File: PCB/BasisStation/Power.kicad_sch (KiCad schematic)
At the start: 5 parts, among them SW1 SW_SPST

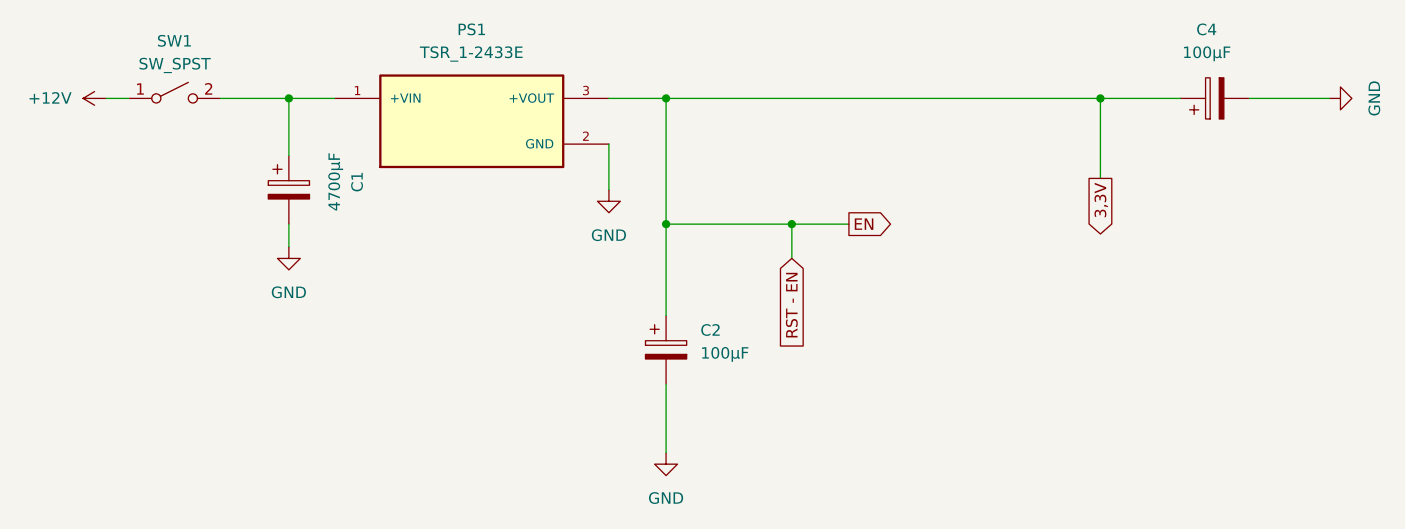
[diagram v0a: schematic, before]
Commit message: Schaltplan angepasst
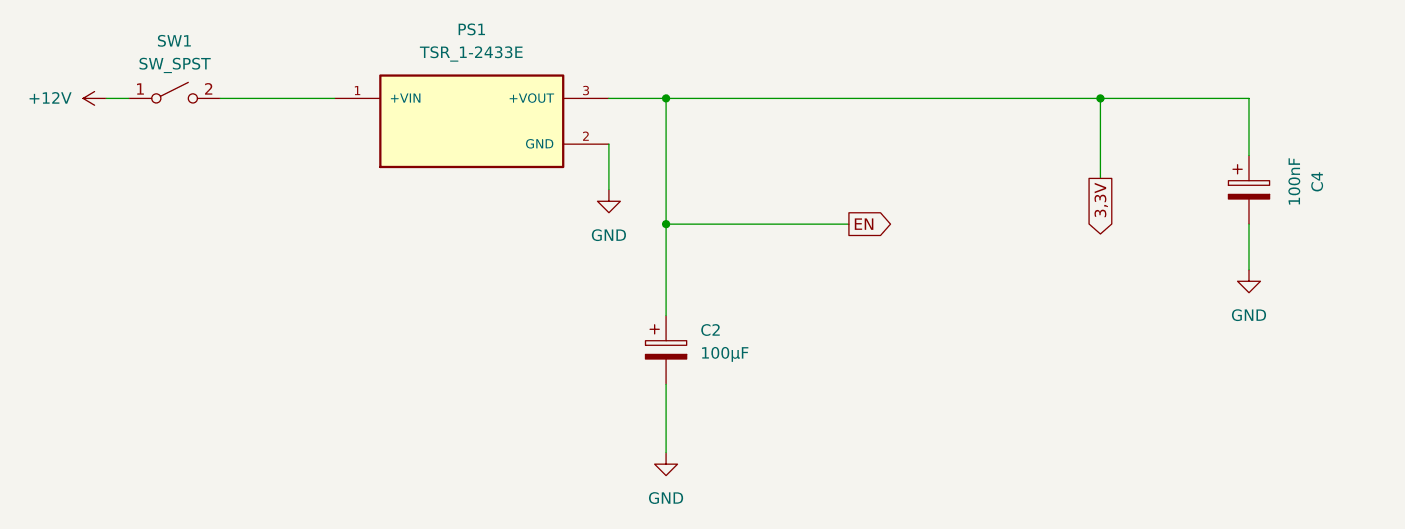
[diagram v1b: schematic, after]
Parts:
- removed C1: 4700µF, CUSTOM_Footprint:CAPAE530X565N, symbol Device:C_Polarized
- C4: value 100µF -> 100nF
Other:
- moved on the sheet: C4
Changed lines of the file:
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@@
-	)
-	(junction
-		(at 115.57 114.3)
-		(diameter 0)
-		(color 0 0 0 0)
-	)
-	(junction
-		(at 59.69 100.33)
-		(diameter 0)
-		(color 0 0 0 0)
 	)
 	(junction
@@
 	(wire
 		(pts
-			(xy 101.6 114.3) (xy 115.57 114.3)
-		)
-		(stroke
-			(width 0)
-			(type default)
-		)
-	)
-	(wire
-		(pts
-			(xy 59.69 100.33) (xy 59.69 106.68)
+			(xy 101.6 114.3) (xy 121.92 114.3)
 		)
 		(stroke
@@
 	(wire
 		(pts
-			(xy 59.69 100.33) (xy 64.77 100.33)
+			(xy 52.07 100.33) (xy 64.77 100.33)
 		)
 		(stroke
@@
 	(wire
 		(pts
-			(xy 52.07 100.33) (xy 59.69 100.33)
-		)
-		(stroke
-			(width 0)
-			(type default)
-		)
-	)
-	(wire
-		(pts
-			(xy 115.57 114.3) (xy 115.57 118.11)
+			(xy 166.37 106.68) (xy 166.37 100.33)
 		)
 		(stroke
@@
 	(wire
 		(pts
-			(xy 121.92 114.3) (xy 115.57 114.3)
-		)
-		(stroke
-			(width 0)
-			(type default)
-		)
-	)
-	(wire
-		(pts
 			(xy 101.6 114.3) (xy 101.6 124.46)
 		)
@@
 	(wire
 		(pts
-			(xy 166.37 100.33) (xy 175.26 100.33)
-		)
-		(stroke
-			(width 0)
-			(type default)
-		)
-	)
-	(wire
-		(pts
 			(xy 95.25 100.33) (xy 101.6 100.33)
 		)
@@
 	(wire
 		(pts
-			(xy 149.86 100.33) (xy 158.75 100.33)
-		)
-		(stroke
-			(width 0)
-			(type default)
-		)
-	)
-	(wire
-		(pts
-			(xy 59.69 116.84) (xy 59.69 114.3)
+			(xy 149.86 100.33) (xy 166.37 100.33)
+		)
+		(stroke
+			(width 0)
+			(type default)
+		)
+	)
+	(wire
+		(pts
+			(xy 166.37 114.3) (xy 166.37 119.38)
 		)
 		(stroke
@@
 				)
 				(justify left)
-				(hide yes)
-			)
-		)
-	)
-	(global_label "RST - EN"
-		(shape input)
-		(at 115.57 118.11 270)
-		(fields_autoplaced yes)
-		(effects
-			(font
-				(size 1.27 1.27)
-			)
-			(justify right)
-		)
-		(property "Intersheetrefs" "${INTERSHEET_REFS}"
-			(at 115.57 130.5294 90)
-			(effects
-				(font
-					(size 1.27 1.27)
-				)
-				(justify right)
 				(hide yes)
 			)
@@
 	)
 	(symbol
-		(lib_id "power:GND")
-		(at 59.69 116.84 0)
-		(unit 1)
-		(exclude_from_sim no)
-		(in_bom yes)
-		(on_board yes)
-		(dnp no)
-		(fields_autoplaced yes)
-		(property "Reference" "#PWR03"
-			(at 59.69 123.19 0)
-			(effects
-				(font
-					(size 1.27 1.27)
-				)
-				(hide yes)
-			)
-		)
-		(property "Value" "GND"
-			(at 59.69 121.92 0)
-			(effects
-				(font
-					(size 1.27 1.27)
-				)
-			)
-		)
-		(property "Footprint" ""
-			(at 59.69 116.84 0)
-			(effects
-				(font
-					(size 1.27 1.27)
-				)
-				(hide yes)
-			)
-		)
-		(property "Datasheet" ""
-			(at 59.69 116.84 0)
-			(effects
-				(font
-					(size 1.27 1.27)
-				)
-				(hide yes)
-			)
-		)
-		(property "Description" "Power symbol creates a global label with name \"GND\" , ground"
-			(at 59.69 116.84 0)
-			(effects
-				(font
-					(size 1.27 1.27)
-				)
-				(hide yes)
-			)
-		)
-		(pin "1"
-		)
-		(instances
-			(project "BasisStation"
-				(path "/cc03a18a-a128-4e00-a998-441923eeacd1/95bbc6e9-cea3-48d2-a467-ede743e61415"
-					(reference "#PWR03")
-					(unit 1)
-				)
-			)
-		)
-	)
-	(symbol
-		(lib_id "Device:C_Polarized")
-		(at 59.69 110.49 0)
-		(unit 1)
-		(exclude_from_sim no)
-		(in_bom yes)
-		(on_board yes)
-		(dnp no)
-		(fields_autoplaced yes)
-		(property "Reference" "C1"
-			(at 67.31 109.601 90)
-			(effects
-				(font
-					(size 1.27 1.27)
-				)
-			)
-		)
-		(property "Value" "4700µF"
-			(at 64.77 109.601 90)
-			(effects
-				(font
-					(size 1.27 1.27)
-				)
-			)
-		)
-		(property "Footprint" "CUSTOM_Footprint:CAPAE530X565N"
-			(at 60.6552 114.3 0)
-			(effects
-				(font
-					(size 1.27 1.27)
-				)
-				(hide yes)
-			)
-		)
-		(property "Datasheet" "https://www.mouser.de/c/passive-components/capacitors/aluminum-electrolytic-capacitors/aluminum-electrolytic-capacitors-smd/?capacitance=4700%20uF&m=Wurth%20Elektronik"
-			(at 59.69 110.49 0)
-			(effects
-				(font
-					(size 1.27 1.27)
-				)
-				(hide yes)
-			)
-		)
-		(property "Description" "Polarized capacitor"
-			(at 59.69 110.49 0)
-			(effects
-				(font
-					(size 1.27 1.27)
-				)
-				(hide yes)
-			)
-		)
-		(pin "1"
-		)
-		(pin "2"
-		)
-		(instances
-			(project "BasisStation"
-				(path "/cc03a18a-a128-4e00-a998-441923eeacd1/95bbc6e9-cea3-48d2-a467-ede743e61415"
-					(reference "C1")
-					(unit 1)
-				)
-			)
-		)
-	)
-	(symbol
 		(lib_id "power:VCC")
 		(at 39.37 100.33 90)
@@
 	(symbol
 		(lib_id "Device:C_Polarized")
-		(at 162.56 100.33 90)
+		(at 166.37 110.49 0)
 		(unit 1)
 		(exclude_from_sim no)
@@
 		(fields_autoplaced yes)
 		(property "Reference" "C4"
-			(at 161.671 92.71 90)
-			(effects
-				(font
-					(size 1.27 1.27)
-				)
-			)
-		)
-		(property "Value" "100µF"
-			(at 161.671 95.25 90)
+			(at 173.99 109.601 90)
+			(effects
+				(font
+					(size 1.27 1.27)
+				)
+			)
+		)
+		(property "Value" "100nF"
+			(at 171.45 109.601 90)
 			(effects
 				(font
@@
 		)
 		(property "Footprint" "CUSTOM_Footprint:CAPAE1030X1050N"
-			(at 166.37 99.3648 0)
+			(at 167.3352 114.3 0)
 			(effects
 				(font
@@
 		)
 		(property "Datasheet" "chrome-extension://efaidnbmnnnibpcajpcglclefindmkaj/https://www.we-online.com/components/products/datasheet/865060343005.pdf"
-			(at 162.56 100.33 0)
+			(at 166.37 110.49 0)
 			(effects
 				(font
@@
 		)
 		(property "Description" "Polarized capacitor"
-			(at 162.56 100.33 0)
+			(at 166.37 110.49 0)
 			(effects
 				(font
@@
 	(symbol
 		(lib_id "power:GND")
-		(at 175.26 100.33 90)
+		(at 166.37 119.38 0)
 		(unit 1)
 		(exclude_from_sim no)
@@
 		(fields_autoplaced yes)
 		(property "Reference" "#PWR013"
-			(at 181.61 100.33 0)
+			(at 166.37 125.73 0)
 			(effects
 				(font
@@
 		)
 		(property "Value" "GND"
-			(at 180.34 100.33 0)
+			(at 166.37 124.46 0)
 			(effects
 				(font
@@
 		)
 		(property "Footprint" ""
-			(at 175.26 100.33 0)
+			(at 166.37 119.38 0)
 			(effects
 				(font
@@
 		)
 		(property "Datasheet" ""
-			(at 175.26 100.33 0)
+			(at 166.37 119.38 0)
 			(effects
 				(font
@@
 		)
 		(property "Description" "Power symbol creates a global label with name \"GND\" , ground"
-			(at 175.26 100.33 0)
-			(effects
-				(font
+			(at 166.37 119.38 0)
+			(effects
+				(font
